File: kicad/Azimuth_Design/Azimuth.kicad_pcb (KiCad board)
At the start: 2 copper layers, 35.9 x 20.1 mm, 21 parts, among them IC1 BNO086, U1 XIAO-ESP32-C3

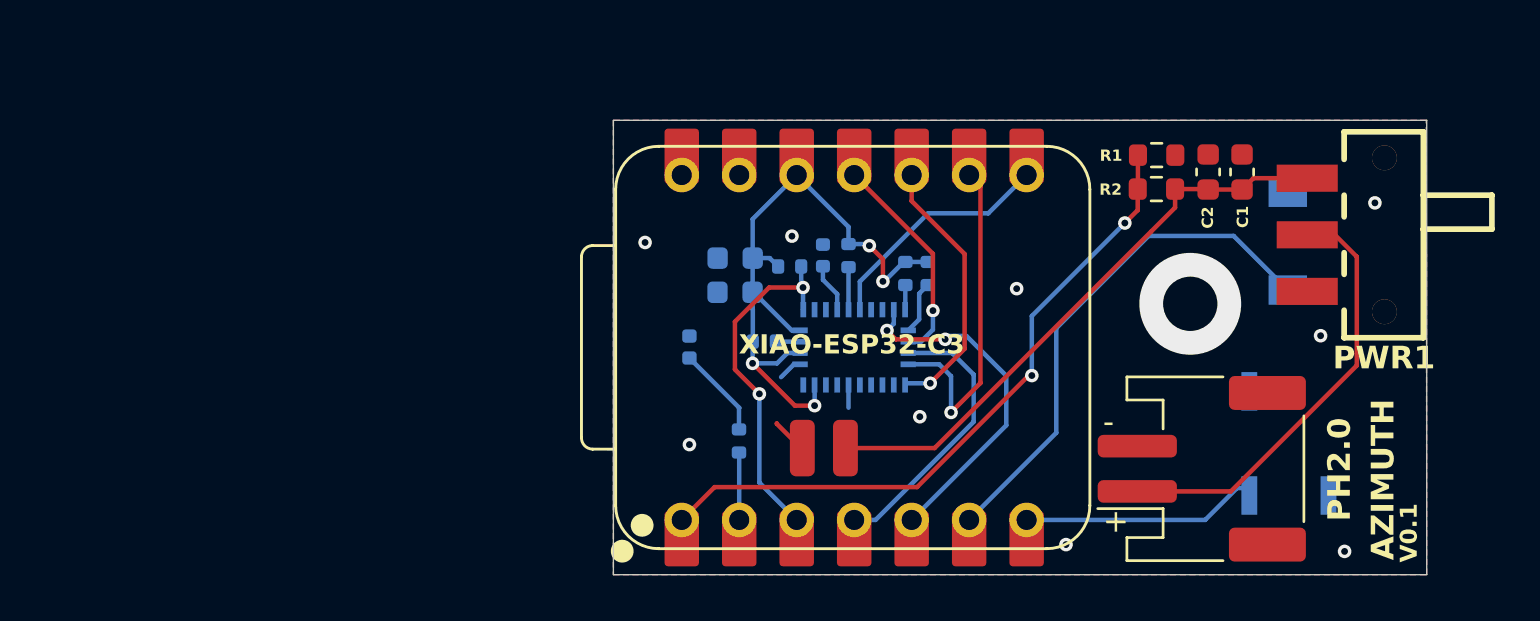
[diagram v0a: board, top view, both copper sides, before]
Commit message: new PCB design almost done, big doc update
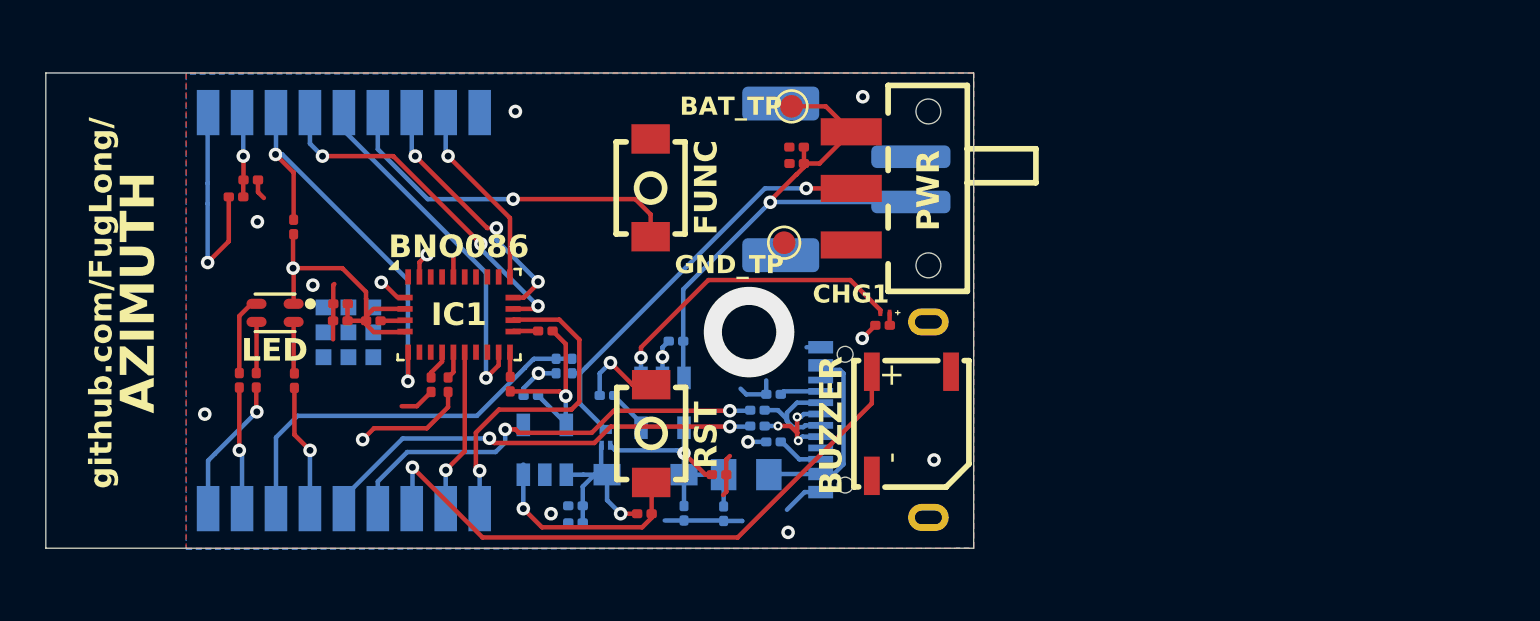
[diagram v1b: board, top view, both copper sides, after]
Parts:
- removed BUZZER1: MLT-5020, 1_MyFootPrints:BUZ-SMD_L5.0-W5.5-P4.60
- removed FUNC1: HX 3X4X2-2P-1.6N TACTILE SWITCH, 1_MyFootPrints:KEY-SMD_L4.0-W3.0-LS4.9-1
- removed LED1: LED, LED_SMD:LED_0402_1005Metric
- removed PWR1: K3-1280S-K1, 1_MyFootPrints:SW-SMD_K3-1280S-K1
- added BAT_TP: DNP, TestPoint:TestPoint_Pad_D1.0mm, F.Cu at (140.4, 82.0)
- added BUZZER: MLT-5020, 1_MyFootPrints:BUZ-SMD_L5.0-W5.5-P4.60, F.Cu at (145.8, 96.0)
- added C10: 0.1uf, Capacitor_SMD:C_0201_0603Metric, F.Cu at (120.5, 91.5)
- added C11: 100nf, Capacitor_SMD:C_0201_0603Metric, F.Cu at (124.5, 94.3)
- added C12: 100nf, Capacitor_SMD:C_0201_0603Metric, F.Cu at (116.6, 85.2)
- added C6: 2.2uF, Capacitor_SMD:C_0201_0603Metric, B.Cu at (128.9, 94.8)
- added C7: 2.2uF, Capacitor_SMD:C_0201_0603Metric, F.Cu at (137.2, 98.2)
- added C8: 10uF, Capacitor_SMD:C_0201_0603Metric, B.Cu at (135.3, 92.3)
- added C9: 10uf, Capacitor_SMD:C_0201_0603Metric, F.Cu at (120.5, 90.7)
- added CHG1: XL-0201SURC, 1_MyFootPrints:LED-SMD_L0.65-W0.35-P0.41_XL-0201SURC, F.Cu at (144.6, 91.1)
- added D1: MBR0530_C5204746, 1_MyFootPrints:SOD-123_L2.7-W1.6-LS3.7-RD-1, B.Cu at (134.0, 98.2)
- added F1: 0805L050WR, 1_MyFootPrints:R0805, B.Cu at (138.4, 98.2)
- added FUNC: HX 3X4X2-2P-1.6N TACTILE SWITCH, 1_MyFootPrints:KEY-SMD_L4.0-W3.0-LS4.9-1, F.Cu at (134.2, 85.6)
- added GND_TP: DNP, TestPoint:TestPoint_Pad_D1.0mm, F.Cu at (140.1, 88.0)
- added J1: TYPE-C 16PIN 2MD(073), 1_MyFootPrints:USB-C-SMD_TYPE-C-6PIN-2MD-073, B.Cu at (144.1, 95.8)
- added LED: TZ-P4-1615RGBTCA1-0.55T, rgb_led_C779813:LED-SMD_4P-L1.6-W1.5-BR_TZ-P4-1615, F.Cu at (117.6, 91.1)
- added PWR: K3-1280S-K1, 1_MyFootPrints:SW-SMD_K3-1280S-K1, F.Cu at (143.1, 85.6)
- added Q1: LP0404N3T5G, 1_MyFootPrints:SOT-883-3_L1.0-W0.6-BR, B.Cu at (132.2, 96.6)
- added R10: 5.1K, Resistor_SMD:R_0201_0603Metric, B.Cu at (139.7, 96.8)
- added R11: 22R, Resistor_SMD:R_0201_0603Metric, B.Cu at (138.9, 96.1)
- added R12: 22R, Resistor_SMD:R_0201_0603Metric, B.Cu at (138.9, 95.4)
- added R13: 10k, Resistor_SMD:R_0201_0603Metric, F.Cu at (122.0, 91.5)
- added R14: 10k, Resistor_SMD:R_0201_0603Metric, F.Cu at (118.5, 87.3)
- added R15: 10k, Resistor_SMD:R_0201_0603Metric, F.Cu at (125.3, 94.3)
- added R16: 4.7k, Resistor_SMD:R_0201_0603Metric, F.Cu at (128.0, 94.2)
- added R17: 4.7k, Resistor_SMD:R_0201_0603Metric, F.Cu at (129.6, 91.9)
- added R18: 10k, Resistor_SMD:R_0201_0603Metric, F.Cu at (115.9, 86.0)
- added R19: 10k, Resistor_SMD:R_0201_0603Metric, F.Cu at (133.9, 100.0)
- added R9: 5.1K, Resistor_SMD:R_0201_0603Metric, B.Cu at (139.7, 94.7)
- added RST: HX 3X4X2-2P-1.6N TACTILE SWITCH, 1_MyFootPrints:KEY-SMD_L4.0-W3.0-LS4.9-1, F.Cu at (134.2, 96.4)
- added U2: TLV75733PDBVR, 1_MyFootPrints:SOT-23-5_L2.9-W1.6-P0.95-LS2.8-BL, B.Cu at (129.6, 97.2)
- added U3: TP4054_C5381776, 1_MyFootPrints:SOT-23-5_L2.9-W1.6-P0.95-LS2.8-BR, B.Cu at (134.8, 95.1)
- C1, C2: footprint Capacitor_SMD:C_0603_1608Metric -> Capacitor_SMD:C_0201_0603Metric
- C3: value 10uf -> 100nF; footprint Capacitor_SMD:C_0603_1608Metric -> Capacitor_SMD:C_0201_0603Metric
- C4: value 0.1uf -> 2.2uF; footprint Capacitor_SMD:C_0603_1608Metric -> Capacitor_SMD:C_0201_0603Metric
- C5: value 100nf -> 2.2uF; footprint Capacitor_SMD:C_0402_1005Metric -> Capacitor_SMD:C_0201_0603Metric
- IC1: moved to F.Cu
- PH2.0: moved to B.Cu
- R1, R2: footprint Resistor_SMD:R_0603_1608Metric -> Resistor_SMD:R_0201_0603Metric; moved to B.Cu
- R3: value 470R -> 100k; footprint Resistor_SMD:R_0402_1005Metric -> Resistor_SMD:R_0201_0603Metric
- R4: value 10k -> 2.5k; footprint Resistor_SMD:R_0402_1005Metric -> Resistor_SMD:R_0201_0603Metric
- R5: value 10k -> 150R; footprint Resistor_SMD:R_0402_1005Metric -> Resistor_SMD:R_0201_0603Metric; moved to F.Cu
- R6: value 10k -> 680R; footprint Resistor_SMD:R_0402_1005Metric -> Resistor_SMD:R_0201_0603Metric; moved to F.Cu
- R7, R8: value 4.7k -> 150R; footprint Resistor_SMD:R_0402_1005Metric -> Resistor_SMD:R_0201_0603Metric; moved to F.Cu
- U1: value XIAO-ESP32-C3 -> ESP32-C3-WROOM-02-N4(4MB); footprint 1_MyFootPrints:XIAO-ESP32-C3-DIP-SMD -> 1_MyFootPrints:BULETM-SMD_ESPRESSIF_ESP32-C3-WROOM-02-N4-4MB; moved to B.Cu
- moved R8 30.8 mm to (116.0, 94.1), turned to 90 degrees
- moved R7 29.1 mm to (116.8, 94.1), turned to 90 degrees
- moved R1 28.1 mm to (130.1, 93.5), turned to -90 degrees
- moved R2 27.0 mm to (130.8, 93.5), turned to -90 degrees
- moved R6 25.1 mm to (118.5, 94.1)
- moved U1 22.6 mm to (120.7, 91.0), turned to -90 degrees
- moved PH2.0 20.3 mm to (142.9, 85.2)
- moved G*** 20.0 mm to (132.6, 86.2)
- moved C1 19.7 mm to (140.7, 83.8), turned to 0 degrees
- moved C2 18.2 mm to (140.7, 84.5), turned to 180 degrees
- moved IC1 17.5 mm to (125.8, 91.2)
- moved C5 16.1 mm to (130.9, 100.4), turned to 180 degrees
- moved C4 13.0 mm to (130.9, 99.6), turned to 180 degrees
- moved C3 9.80 mm to (137.4, 100.0), turned to 90 degrees
- moved R4 7.35 mm to (132.3, 94.8), turned to 180 degrees
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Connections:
- net Net-(IC1-H_CSN) renamed /IO5
- net Net-(IC1-H_INTN) renamed /IO6
- C1 pad 2: vcc -> /VBAT
- C2 pad 1: vcc -> /VBAT
- C3 pad 2: Net-(IC1-PS1) -> /USB_5V
- C4 pad 1: GND -> /VIN
- C4 pad 2: Net-(IC1-PS1) -> GND
- C5 pad 1: GND -> /VIN
- C5 pad 2: Net-(IC1-CAP) -> GND
- IC1 pad 11: Net-(IC1-NRST) -> /IO20
- IC1 pad 17: Net-(IC1-SA0/H_MOSI) -> /IO10
- IC1 pad 19: Net-(IC1-H_SCL/SCK/RX) -> /IO8
- IC1 pad 20: Net-(IC1-H_SDA/H_MISO/TX) -> /IO9
- IC1 pad 28: Net-(IC1-PS1) -> /3V3
- IC1 pad 3: Net-(IC1-PS1) -> /3V3
- IC1 pad 5: Net-(IC1-PS1) -> /3V3
- IC1 pad 6: Net-(IC1-PS0/WAKE) -> /IO4
- PH2.0 pad 1: /Bat+ -> /VBAT
- R1 pad 1: Net-(U1-GPIO2_A0_D0) -> /IO2
- R2 pad 1: Net-(U1-GPIO2_A0_D0) -> /IO2
- R2 pad 2: vcc -> /VBAT_SW
- R3 pad 1: Net-(LED1-A) -> GND
- R3 pad 2: Net-(U1-GPIO3_A1_D1) -> /USB_5V
- R4 pad 1: Net-(IC1-PS1) -> Net-(U3-PROG)
- R4 pad 2: Net-(IC1-BOOTN) -> GND
- R5 pad 1: Net-(IC1-PS1) -> /3V3
- R5 pad 2: Net-(IC1-PS0/WAKE) -> Net-(CHG1-A)
- R6 pad 1: Net-(IC1-PS1) -> Net-(LED1---Pad2)
- R6 pad 2: Net-(IC1-CLKSEL0) -> /IO3
- R7 pad 1: Net-(IC1-PS1) -> /IO0
- R7 pad 2: Net-(IC1-ENV_SCL) -> Net-(LED1---Pad3)
- R8 pad 1: Net-(IC1-PS1) -> /IO1
- R8 pad 2: Net-(IC1-ENV_SDA) -> Net-(LED1---Pad4)
- U1 pad 1: Net-(U1-GPIO2_A0_D0) -> /3V3
- U1 pad 10: Net-(IC1-H_SDA/H_MISO/TX) -> /IO10
- U1 pad 11: Net-(IC1-SA0/H_MOSI) -> /IO20
- U1 pad 12: Net-(IC1-PS1) -> /IO21
- U1 pad 13: GND -> /Data-
- U1 pad 14: unconnected-(U1-VBUS-Pad14) -> /Data+
- U1 pad 15: vcc -> /IO3
- U1 pad 16: GND -> /IO2
- U1 pad 2: Net-(U1-GPIO3_A1_D1) -> Net-(U1-EN)
- U1 pad 3: Net-(IC1-PS0/WAKE) -> /IO4
- U1 pad 6: Net-(U1-GPIO7_D5_SCL) -> /IO7
- U1 pad 7: Net-(BUZZER1-+) -> /IO8
- U1 pad 8: Net-(IC1-NRST) -> /IO9
- U1 pad 9: Net-(IC1-H_SCL/SCK/RX) -> GND
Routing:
- net /3V3: track 0.00 -> 39.4 mm, vias 0 -> 6
- net Net-(U1-GPIO2_A0_D0): track 29.8 -> 0.00 mm, vias 2 -> 0
- net Net-(IC1-PS1): track 29.4 -> 0.00 mm, vias 4 -> 0
- net /IO21: track 0.00 -> 27.3 mm, vias 0 -> 1
- net vcc: track 25.8 -> 0.00 mm
- net /VBAT: track 0.00 -> 25.0 mm, vias 0 -> 1
- net Net-(U1-GPIO7_D5_SCL): track 23.0 -> 0.00 mm
- net /Bat+: track 21.2 -> 0.00 mm
- net GND: track 3.66 -> 24.9 mm, vias 10 -> 14
- net /Data+: track 0.00 -> 19.9 mm, vias 0 -> 2
- net /Data-: track 0.00 -> 19.4 mm, vias 0 -> 2
- net /IO4: track 0.00 -> 19.0 mm, vias 0 -> 2
- net /VBAT_SW: track 0.00 -> 18.7 mm, vias 0 -> 1
- net /IO2: track 0.00 -> 17.7 mm
- net /IO7: track 0.00 -> 15.9 mm, vias 0 -> 1
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- added copper zone on In2.Cu, net /3V3
- added copper zone on In1.Cu, net GND
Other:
- board size 35.9 x 20.1 mm -> 41 x 21 mm
- copper layers 2 -> 4
- board text added: "github.com/FugLong/"

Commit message: PCB locked in for now, docs updated
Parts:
- added D2: B5819WS, 1_MyFootPrints:SOD-323_L1.8-W1.3-LS2.5-RD, F.Cu at (142.1, 95.2)
- added Q2: AO3400A, 1_MyFootPrints:SOT-23-3_L2.9-W1.3-P1.90-LS2.4-BR, F.Cu at (140.2, 98.7)
- added R20: 330R, Resistor_SMD:R_0201_0603Metric, F.Cu at (136.9, 99.7)
- added R21: 100K, Resistor_SMD:R_0201_0603Metric, F.Cu at (137.6, 99.7)
- C1, C10, C2, C8, C9: footprint Capacitor_SMD:C_0201_0603Metric -> Capacitor_SMD:C_0402_1005Metric
- R1, R2: footprint Resistor_SMD:R_0201_0603Metric -> Resistor_SMD:R_0402_1005Metric
- R4: value 2.5k -> 2K
- moved R5 0.60 mm to (144.7, 92.2)
- moved C1 0.53 mm to (140.2, 83.5)
- moved C2 0.49 mm to (140.2, 84.5)
- moved CHG 0.42 mm to (144.4, 91.5)
- moved R2 0.28 mm to (131.0, 93.5)
- moved R1 0.28 mm to (129.8, 93.5)
- moved C7 0.25 mm to (137.2, 98.5)
- moved C9 0.22 mm to (120.3, 90.6)
- moved C10 0.21 mm to (120.3, 91.5)
- moved C8 0.15 mm to (135.2, 92.3)
- renumbered BAT_TP to BAT_0, CHG1 to CHG, GND_TP to GND_0
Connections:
- BUZZER pad 1: /IO21 -> /3V3
- BUZZER pad 2: GND -> Net-(BUZZER1--)
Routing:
- net /IO21: track 27.3 -> 16.7 mm
- net Net-(BUZZER1--): track 0.00 -> 5.43 mm
- net /3V3: track 39.4 -> 43.3 mm
- net Net-(Q2-G): track 0.00 -> 3.03 mm
- net GND: track 24.9 -> 27.3 mm
- net /VBAT: track 25.0 -> 25.7 mm

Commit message: PCB finalized? :O
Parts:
- removed BAT_0, GND_0: DNP, TestPoint:TestPoint_Pad_D1.0mm
- added Q3: AO3401A, 1_MyFootPrints:SOT-23-3_L2.9-W1.3-P1.90-LS2.4-BR, F.Cu at (137.9, 82.4)
- added R22: 100k, Resistor_SMD:R_0201_0603Metric, F.Cu at (140.3, 83.3)
- C3: value 100nF -> 100nf
- C4, C5, C6, C7: value 2.2uF -> 2.2uf
- C8: value 10uF -> 10uf
- R1, R2: value 220K -> 220k
- R10, R9: value 5.1K -> 5.1k
- R21: value 100K -> 100k
- moved R14 8.89 mm to (120.3, 96.0)
- moved C1 0.91 mm to (139.8, 84.3)
- moved C2 0.91 mm to (139.8, 85.3)
- moved R19 0.27 mm to (133.9, 99.7)
- renumbered BUZZER to BUZZER1, CHG to CHG1, FUNC to FUNC1, LED to LED1, PWR to PWR1, RST to RST1
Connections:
- IC1 pad 6: /IO4 -> /IO2
- PH2.0 pad 1: /VBAT -> GND
- PH2.0 pad 2: GND -> Net-(PH2.0-Pin_2)
- R1 pad 1: /IO2 -> /IO4
- R14 pad 2: /IO4 -> /IO2
- R2 pad 1: /IO2 -> /IO4
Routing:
- net Net-(PH2.0-Pin_2): track 0.00 -> 12.8 mm, vias 0 -> 1
- net /IO2: track 17.7 -> 11.3 mm, vias 0 -> 1
- net /VBAT: track 25.7 -> 20.6 mm
- net GND: track 27.3 -> 30.6 mm, vias 14 -> 17
- net Net-(Q3-G): track 0.00 -> 1.08 mm
- net Net-(U2-EN): track 9.30 -> 8.42 mm
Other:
- board size 41 x 21 mm -> 35 x 21 mm
- board text added: "!"
- board text added: "github.com/FugLong/Azimuth"
- board text removed: "AZIMUTH"
- board text removed: "github.com/FugLong/"

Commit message: Manufacturing optimizations
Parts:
- R6: value 680R -> 220R
- R7: value 150R -> 100R
- R8: value 150R -> 68R
- moved R9 0.79 mm to (140.3, 94.2)
- moved R11 0.64 mm to (138.3, 96.1)
- moved R12 0.51 mm to (138.4, 95.4)
- moved R10 0.26 mm to (139.4, 96.8)
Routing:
- net GND: track 30.6 -> 34.2 mm
- net /DP: track 4.79 -> 6.04 mm
- net /DN: track 4.99 -> 5.69 mm
- net Net-(J1-CC1): track 1.82 -> 1.25 mm
- net /Data+: track 20.2 -> 19.7 mm
- net /Data-: track 19.3 -> 18.8 mm
